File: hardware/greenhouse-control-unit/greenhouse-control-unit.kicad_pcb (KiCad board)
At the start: 4 copper layers, 150 x 90 mm, 53 parts, among them J1 Molex_KK-396_01x02, J10 Conn_ESP32_DevKitV1_Female, J11 Conn_01x05_Female, J12 Conn_01x05_Female, J13 Molex_KK-396_01x12, J14 Molex_KK-254_01x12, J2 Molex_KK-396_01x02, J3 Beep_Jumper, J4 Conn_01x01_Male, J5 Conn_01x01_Male, J6 Conn_01x01_Male, J7 Conn_01x01_Male, J8 Conn_01x09, J9 Conn_01x05_Female, Q1 BC547, Q2 BC547, Q3 BC337, Q4 BC547, Q5 2N3906, Q6 BC547, Q7 BC337, U1 PCF8574

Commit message: Add power in/out silkscreen text
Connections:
- J1 pad 1: /Batt+12V -> +12V

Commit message: Add + pin text to PCB
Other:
- board text added: "+"
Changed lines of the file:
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@@
   (gr_rect (start 104.14 104.278) (end 94.017 128.778) (layer "Dwgs.User") (width 0.15) (fill none))
   (gr_rect locked (start 72.1356 44.4645) (end 222.1356 134.4645) (layer "Edge.Cuts") (width 0.2) (fill none))
+  (gr_text "+" (at 191.7 45.538) (layer "F.SilkS")
+    (effects (font (size 1 1) (thickness 0.15)))
+  )
+  (gr_text "+" (at 142.2 45.538) (layer "F.SilkS")
+    (effects (font (size 1 1) (thickness 0.15)))
+  )
+  (gr_text "+" (at 173.95 45.538) (layer "F.SilkS")
+    (effects (font (size 1 1) (thickness 0.15)))
+  )
   (gr_text "OUT" (at 208.9284 104.1015) (layer "F.SilkS")
     (effects (font (size 1.5 1.5) (thickness 0.25)))
@@
     (effects (font (size 1.5 1.5) (thickness 0.3)) (justify left))
   )
+  (gr_text "+" (at 158.15 45.538) (layer "F.SilkS")
+    (effects (font (size 1 1) (thickness 0.15)))
+  )
+  (gr_text "+" (at 150.1 45.538) (layer "F.SilkS")
+    (effects (font (size 1 1) (thickness 0.15)))
+  )
   (gr_text "5V buck module" (at 208.806 60.706) (layer "F.SilkS")
     (effects (font (size 1.5 1.5) (thickness 0.25)))
+  )
+  (gr_text "+" (at 181.8 45.538) (layer "F.SilkS")
+    (effects (font (size 1 1) (thickness 0.15)))
   )
   (gr_text "Greenhouse Control Unit" (at 181.61 127.508) (layer "F.SilkS")
@@
     (effects (font (size 1.5 1.5) (thickness 0.25)))
   )
+  (gr_text "+" (at 201.85 45.538) (layer "F.SilkS")
+    (effects (font (size 1 1) (thickness 0.15)))
+  )
+  (gr_text "+" (at 165.85 45.538) (layer "F.SilkS")
+    (effects (font (size 1 1) (thickness 0.15)))
+  )
   (segment (start 102.616 49.53) (end 102.616 51.435) (width 0.5) (layer "F.Cu") (net 1))

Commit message: Fixed missing GND on MCU
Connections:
- J10 pad 17: unconnected-(J10-Pad17) -> GND
- J10 pad 2: unconnected-(J10-Pad2) -> GND
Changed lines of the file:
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@@
   (net 57 "Net-(J3-Pad1)")
   (net 58 "unconnected-(J3-Pad3)")
-  (net 59 "unconnected-(J10-Pad2)")
-  (net 60 "unconnected-(J10-Pad3)")
-  (net 61 "unconnected-(J10-Pad4)")
-  (net 62 "unconnected-(J10-Pad7)")
-  (net 63 "unconnected-(J10-Pad8)")
-  (net 64 "unconnected-(J10-Pad9)")
-  (net 65 "unconnected-(J10-Pad10)")
-  (net 66 "unconnected-(J10-Pad11)")
-  (net 67 "unconnected-(J10-Pad13)")
-  (net 68 "unconnected-(J10-Pad14)")
-  (net 69 "unconnected-(J10-Pad15)")
-  (net 70 "unconnected-(J10-Pad17)")
-  (net 71 "unconnected-(J10-Pad18)")
-  (net 72 "unconnected-(J10-Pad19)")
-  (net 73 "unconnected-(J10-Pad21)")
-  (net 74 "unconnected-(J10-Pad22)")
-  (net 75 "unconnected-(J10-Pad27)")
-  (net 76 "unconnected-(J10-Pad28)")
+  (net 59 "unconnected-(J10-Pad3)")
+  (net 60 "unconnected-(J10-Pad4)")
+  (net 61 "unconnected-(J10-Pad7)")
+  (net 62 "unconnected-(J10-Pad8)")
+  (net 63 "unconnected-(J10-Pad9)")
+  (net 64 "unconnected-(J10-Pad10)")
+  (net 65 "unconnected-(J10-Pad11)")
+  (net 66 "unconnected-(J10-Pad13)")
+  (net 67 "unconnected-(J10-Pad14)")
+  (net 68 "unconnected-(J10-Pad15)")
+  (net 69 "unconnected-(J10-Pad18)")
+  (net 70 "unconnected-(J10-Pad19)")
+  (net 71 "unconnected-(J10-Pad21)")
+  (net 72 "unconnected-(J10-Pad22)")
+  (net 73 "unconnected-(J10-Pad27)")
+  (net 74 "unconnected-(J10-Pad28)")
   (footprint "Connector_PinHeader_2.54mm:PinHeader_1x03_P2.54mm_Vertical" (layer "F.Cu")
     (at 91.1468 71.7296 90)
@@
       (net 3 "+5V") (pinfunction "VIN_5V") (pintype "power_in"))
     (pad "2" thru_hole oval (at -13.3 15.076 180) (size 1.7 1.7) (drill 1) (layers *.Cu *.Mask)
-      (net 59 "unconnected-(J10-Pad2)") (pinfunction "GND") (pintype "power_in+no_connect"))
+      (net 1 "GND") (pinfunction "GND") (pintype "power_in"))
     (pad "3" thru_hole oval (at -13.3 12.536 180) (size 1.7 1.7) (drill 1) (layers *.Cu *.Mask)
-      (net 60 "unconnected-(J10-Pad3)") (pinfunction "D13") (pintype "bidirectional+no_connect"))
+      (net 59 "unconnected-(J10-Pad3)") (pinfunction "D13") (pintype "bidirectional+no_connect"))
     (pad "4" thru_hole oval (at -13.3 9.996 180) (size 1.7 1.7) (drill 1) (layers *.Cu *.Mask)
-      (net 61 "unconnected-(J10-Pad4)") (pinfunction "D12") (pintype "bidirectional+no_connect"))
+      (net 60 "unconnected-(J10-Pad4)") (pinfunction "D12") (pintype "bidirectional+no_connect"))
     (pad "5" thru_hole oval (at -13.3 7.456 180) (size 1.7 1.7) (drill 1) (layers *.Cu *.Mask)
       (net 29 "/HC12_RX") (pinfunction "D14") (pintype "bidirectional"))
@@
       (net 30 "/HC12_TX") (pinfunction "D27") (pintype "bidirectional"))
     (pad "7" thru_hole oval (at -13.3 2.376 180) (size 1.7 1.7) (drill 1) (layers *.Cu *.Mask)
-      (net 62 "unconnected-(J10-Pad7)") (pinfunction "D26") (pintype "bidirectional+no_connect"))
+      (net 61 "unconnected-(J10-Pad7)") (pinfunction "D26") (pintype "bidirectional+no_connect"))
     (pad "8" thru_hole oval (at -13.3 -0.164 180) (size 1.7 1.7) (drill 1) (layers *.Cu *.Mask)
-      (net 63 "unconnected-(J10-Pad8)") (pinfunction "D25") (pintype "bidirectional+no_connect"))
+      (net 62 "unconnected-(J10-Pad8)") (pinfunction "D25") (pintype "bidirectional+no_connect"))
     (pad "9" thru_hole oval (at -13.3 -2.704 180) (size 1.7 1.7) (drill 1) (layers *.Cu *.Mask)
-      (net 64 "unconnected-(J10-Pad9)") (pinfunction "D33") (pintype "bidirectional+no_connect"))
+      (net 63 "unconnected-(J10-Pad9)") (pinfunction "D33") (pintype "bidirectional+no_connect"))
     (pad "10" thru_hole oval (at -13.3 -5.244 180) (size 1.7 1.7) (drill 1) (layers *.Cu *.Mask)
-      (net 65 "unconnected-(J10-Pad10)") (pinfunction "D32") (pintype "bidirectional+no_connect"))
+      (net 64 "unconnected-(J10-Pad10)") (pinfunction "D32") (pintype "bidirectional+no_connect"))
     (pad "11" thru_hole oval (at -13.3 -7.784 180) (size 1.7 1.7) (drill 1) (layers *.Cu *.Mask)
-      (net 66 "unconnected-(J10-Pad11)") (pinfunction "D35") (pintype "bidirectional+no_connect"))
+      (net 65 "unconnected-(J10-Pad11)") (pinfunction "D35") (pintype "bidirectional+no_connect"))
     (pad "12" thru_hole oval (at -13.3 -10.324 180) (size 1.7 1.7) (drill 1) (layers *.Cu *.Mask)
       (net 31 "/VSense") (pinfunction "D34") (pintype "bidirectional"))
     (pad "13" thru_hole oval (at -13.3 -12.864 180) (size 1.7 1.7) (drill 1) (layers *.Cu *.Mask)
-      (net 67 "unconnected-(J10-Pad13)") (pinfunction "VN") (pintype "bidirectional+no_connect"))
+      (net 66 "unconnected-(J10-Pad13)") (pinfunction "VN") (pintype "bidirectional+no_connect"))
     (pad "14" thru_hole oval (at -13.3 -15.404 180) (size 1.7 1.7) (drill 1) (layers *.Cu *.Mask)
-      (net 68 "unconnected-(J10-Pad14)") (pinfunction "VP") (pintype "bidirectional+no_connect"))
+      (net 67 "unconnected-(J10-Pad14)") (pinfunction "VP") (pintype "bidirectional+no_connect"))
     (pad "15" thru_hole oval (at -13.3 -17.944 180) (size 1.7 1.7) (drill 1) (layers *.Cu *.Mask)
-      (net 69 "unconnected-(J10-Pad15)") (pinfunction "EN") (pintype "bidirectional+no_connect"))
+      (net 68 "unconnected-(J10-Pad15)") (pinfunction "EN") (pintype "bidirectional+no_connect"))
     (pad "16" thru_hole rect (at 12.4 17.616 180) (size 1.7 1.7) (drill 1) (layers *.Cu *.Mask)
       (net 4 "+3V3") (pinfunction "3V3") (pintype "power_out"))
     (pad "17" thru_hole oval (at 12.4 15.086) (size 1.7 1.7) (drill 1) (layers *.Cu *.Mask)
-      (net 70 "unconnected-(J10-Pad17)") (pinfunction "GND") (pintype "power_in+no_connect"))
+      (net 1 "GND") (pinfunction "GND") (pintype "power_in"))
     (pad "18" thru_hole oval (at 12.4 12.546) (size 1.7 1.7) (drill 1) (layers *.Cu *.Mask)
-      (net 71 "unconnected-(J10-Pad18)") (pinfunction "D15") (pintype "bidirectional+no_connect"))
+      (net 69 "unconnected-(J10-Pad18)") (pinfunction "D15") (pintype "bidirectional+no_connect"))
     (pad "19" thru_hole oval (at 12.4 10.006) (size 1.7 1.7) (drill 1) (layers *.Cu *.Mask)
-      (net 72 "unconnected-(J10-Pad19)") (pinfunction "D2") (pintype "bidirectional+no_connect"))
+      (net 70 "unconnected-(J10-Pad19)") (pinfunction "D2") (pintype "bidirectional+no_connect"))
     (pad "20" thru_hole oval (at 12.4 7.466) (size 1.7 1.7) (drill 1) (layers *.Cu *.Mask)
       (net 24 "/RFM95_IRQ") (pinfunction "D4") (pintype "bidirectional"))
     (pad "21" thru_hole oval (at 12.4 4.926) (size 1.7 1.7) (drill 1) (layers *.Cu *.Mask)
-      (net 73 "unconnected-(J10-Pad21)") (pinfunction "RX2") (pintype "bidirectional+no_connect"))
+      (net 71 "unconnected-(J10-Pad21)") (pinfunction "RX2") (pintype "bidirectional+no_connect"))
     (pad "22" thru_hole oval (at 12.4 2.386) (size 1.7 1.7) (drill 1) (layers *.Cu *.Mask)
-      (net 74 "unconnected-(J10-Pad22)") (pinfunction "TX2") (pintype "bidirectional+no_connect"))
+      (net 72 "unconnected-(J10-Pad22)") (pinfunction "TX2") (pintype "bidirectional+no_connect"))
     (pad "23" thru_hole oval (at 12.4 -0.154) (size 1.7 1.7) (drill 1) (layers *.Cu *.Mask)
       (net 28 "/RFM95_CS") (pinfunction "D5") (pintype "bidirectional"))
@@
       (net 22 "/I2C_SDA") (pinfunction "D21") (pintype "bidirectional"))
     (pad "27" thru_hole oval (at 12.4 -10.314) (size 1.7 1.7) (drill 1) (layers *.Cu *.Mask)
-      (net 75 "unconnected-(J10-Pad27)") (pinfunction "RXD") (pintype "bidirectional+no_connect"))
+      (net 73 "unconnected-(J10-Pad27)") (pinfunction "RXD") (pintype "bidirectional+no_connect"))
     (pad "28" thru_hole oval (at 12.4 -12.854) (size 1.7 1.7) (drill 1) (layers *.Cu *.Mask)
-      (net 76 "unconnected-(J10-Pad28)") (pinfunction "TXD") (pintype "bidirectional+no_connect"))
+      (net 74 "unconnected-(J10-Pad28)") (pinfunction "TXD") (pintype "bidirectional+no_connect"))
     (pad "29" thru_hole oval (at 12.4 -15.394) (size 1.7 1.7) (drill 1) (layers *.Cu *.Mask)
       (net 23 "/I2C_SCL") (pinfunction "D22") (pintype "bidirectional"))

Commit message: First pass at R4
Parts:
- removed C1: 220uF, Capacitor_THT:CP_Radial_D6.3mm_P2.50mm
- removed J13: Molex_KK-396_01x12, Connector_Molex:Molex_KK-396_A-41791-0012_1x12_P3.96mm_Vertical
- removed J7: Conn_01x01_Male, Connector_Pin:Pin_D1.0mm_L10.0mm
- added C3: 10nF, Capacitor_THT:C_Disc_D4.7mm_W2.5mm_P5.00mm, F.Cu at (137.7, 83.1)
- added F1: Fuse, Fuse:Fuse_Blade_Mini_directSolder, F.Cu at (170.6, 39.1)
- added J15: Molex_KK-396_01x02, Connector_Molex:Molex_KK-396_A-41791-0002_1x02_P3.96mm_Vertical, F.Cu at (199.4, 42.2)
- added Q10: 2N7000, Package_TO_SOT_THT:TO-92_Inline, F.Cu at (110.0, 88.5)
- added Q11: FDP7030BL, Package_TO_SOT_THT:TO-220-3_Horizontal_TabDown, F.Cu at (212.6, 54.3)
- added Q12: FDP7030BL, Package_TO_SOT_THT:TO-220-3_Horizontal_TabDown, F.Cu at (167.9, 54.3)
- added Q13: 2N7002, Package_TO_SOT_SMD:SOT-23, F.Cu at (128.0, 64.4)
- added Q14: STD30NF06LT4, Package_TO_SOT_SMD:TO-252-2, F.Cu at (128.0, 56.1)
- added Q15: 2N7002, Package_TO_SOT_SMD:SOT-23, F.Cu at (143.3, 64.4)
- added Q16: STD30NF06LT4, Package_TO_SOT_SMD:TO-252-2, F.Cu at (143.3, 56.1)
- added Q17: 2N7002, Package_TO_SOT_SMD:SOT-23, F.Cu at (135.6, 64.4)
- added Q18: 2N7002, Package_TO_SOT_SMD:SOT-23, F.Cu at (150.9, 64.4)
- added Q19: STD30NF06LT4, Package_TO_SOT_SMD:TO-252-2, F.Cu at (135.6, 56.1)
- added Q20: STD30NF06LT4, Package_TO_SOT_SMD:TO-252-2, F.Cu at (150.9, 56.1)
- added Q8: FDP7030BL, Package_TO_SOT_THT:TO-220-3_Horizontal_TabDown, F.Cu at (201.4, 54.3)
- added Q9: FDP7030BL, Package_TO_SOT_THT:TO-220-3_Horizontal_TabDown, F.Cu at (179.1, 54.3)
- added R18: 0R1, Resistor_SMD:R_2512_6332Metric_Pad1.40x3.35mm_HandSolder, F.Cu at (159.8, 46.0)
- added R19: 10k, Resistor_THT:R_Axial_DIN0207_L6.3mm_D2.5mm_P7.62mm_Horizontal, F.Cu at (111.5, 58.2)
- added R20: 10k, Resistor_THT:R_Axial_DIN0207_L6.3mm_D2.5mm_P7.62mm_Horizontal, F.Cu at (99.3, 50.5)
- added R21: 10k, Resistor_THT:R_Axial_DIN0207_L6.3mm_D2.5mm_P7.62mm_Horizontal, F.Cu at (125.5, 83.1)
- added R22: 100k, Resistor_THT:R_Axial_DIN0207_L6.3mm_D2.5mm_P7.62mm_Horizontal, F.Cu at (129.7, 75.8)
- added R23: 10k, Resistor_THT:R_Axial_DIN0207_L6.3mm_D2.5mm_P7.62mm_Horizontal, F.Cu at (108.5, 58.2)
- added R24: 1M, Resistor_THT:R_Axial_DIN0207_L6.3mm_D2.5mm_P7.62mm_Horizontal, F.Cu at (105.4, 50.5)
- added R25: 100k, Resistor_THT:R_Axial_DIN0207_L6.3mm_D2.5mm_P7.62mm_Horizontal, F.Cu at (102.4, 58.2)
- added R26: 10k, Resistor_THT:R_Axial_DIN0207_L6.3mm_D2.5mm_P7.62mm_Horizontal, F.Cu at (96.3, 50.5)
- added R27: 10k, Resistor_THT:R_Axial_DIN0207_L6.3mm_D2.5mm_P7.62mm_Horizontal, F.Cu at (126.4, 68.2)
- added R28: 100k, Resistor_THT:R_Axial_DIN0207_L6.3mm_D2.5mm_P7.62mm_Horizontal, F.Cu at (144.9, 75.9)
- added R29: 10k, Resistor_THT:R_Axial_DIN0207_L6.3mm_D2.5mm_P7.62mm_Horizontal, F.Cu at (141.6, 68.2)
- added R30: 100k, Resistor_THT:R_Axial_DIN0207_L6.3mm_D2.5mm_P7.62mm_Horizontal, F.Cu at (137.3, 75.8)
- added R31: 100k, Resistor_THT:R_Axial_DIN0207_L6.3mm_D2.5mm_P7.62mm_Horizontal, F.Cu at (152.5, 75.8)
- added R32: 10k, Resistor_THT:R_Axial_DIN0207_L6.3mm_D2.5mm_P7.62mm_Horizontal, F.Cu at (134.0, 68.2)
- added R33: 10k, Resistor_THT:R_Axial_DIN0207_L6.3mm_D2.5mm_P7.62mm_Horizontal, F.Cu at (149.2, 68.2)
- added U2: PCF8574, Package_SO:SOIC-16W_7.5x10.3mm_P1.27mm, F.Cu at (135.2, 90.2)
- added U3: ZXCT1107, Package_TO_SOT_SMD:SOT-23, F.Cu at (213.9, 49.5)
- added U4: ZXCT1107, Package_TO_SOT_SMD:SOT-23, F.Cu at (159.8, 50.0)
- D4: value LED -> D; footprint LED_THT:LED_D5.0mm -> Diode_THT:D_DO-41_SOD81_P7.62mm_Horizontal
- D5: value FR107 -> LED; footprint Diode_THT:D_DO-41_SOD81_P7.62mm_Horizontal -> LED_THT:LED_D5.0mm
- J4: value Conn_01x01_Male -> PV Buck; footprint Connector_Pin:Pin_D1.0mm_L10.0mm -> Nick:Buck_Module
- J5: value Conn_01x01_Male -> Conn_01x08_Male; footprint Connector_Pin:Pin_D1.0mm_L10.0mm -> Connector_Molex:Molex_KK-396_A-41791-0008_1x08_P3.96mm_Vertical
- J6: value Conn_01x01_Male -> 5V Buck; footprint Connector_Pin:Pin_D1.0mm_L10.0mm -> Nick:Buck_Module
- Q1, Q4: value BC547 -> 2N7000
- Q3: value BC337 -> TN0702
- Q5: value 2N3906 -> FDP7030BL; footprint Package_TO_SOT_THT:TO-92_Inline -> Package_TO_SOT_THT:TO-220-3_Horizontal_TabDown
- R1: value 33k -> 100k
- R10: value 220k -> 100k
- R12: value 10k -> 0R1; footprint Resistor_THT:R_Axial_DIN0207_L6.3mm_D2.5mm_P7.62mm_Horizontal -> Resistor_SMD:R_2512_6332Metric_Pad1.40x3.35mm_HandSolder
- R3, R8: value 1k -> 10k
- U1: footprint Package_DIP:DIP-16_W7.62mm_Socket -> Package_SO:SOIC-16W_7.5x10.3mm_P1.27mm
- moved D4 139.8 mm to (216.7, 78.2), turned to 180 degrees
- moved J5 94.5 mm to (125.2, 42.4), turned to 0 degrees
- moved R12 86.9 mm to (217.9, 49.5)
- moved Q5 86.9 mm to (190.2, 54.3), turned to 180 degrees
- moved D6 26.9 mm to (193.5, 78.2), turned to 180 degrees
- moved U1 25.4 mm to (135.2, 104.4)
- moved D5 25.0 mm to (77.6, 67.6), turned to -90 degrees
- moved C2 19.9 mm to (137.7, 97.3), turned to 180 degrees
- moved R9 19.7 mm to (114.6, 50.5)
- moved R10 19.5 mm to (117.7, 58.2)
- moved R3 18.9 mm to (117.9, 95.2), turned to 0 degrees
- moved Q4 17.6 mm to (103.6, 88.5)
- moved R16 16.3 mm to (117.9, 98.3)
- moved R5 16.3 mm to (125.5, 92.2)
- moved J1 15.3 mm to (189.5, 42.3)
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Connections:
- net /VSense renamed /Common_VS
- D4 pad 1: GND -> Net-(D4-Pad1)
- D4 pad 2: Net-(D4-Pad2) -> /PV_Vcc
- D5 pad 1: /BattRelayNC_A -> GND
- D5 pad 2: GND -> Net-(D5-Pad2)
- D6 pad 1: /Buck+12V -> Net-(D6-Pad1)
- J1 pad 1: +12V -> /Batt+12V
- J1 pad 2: GND -> /Batt_GND
- J10 pad 10: unconnected-(J10-Pad10) -> /PV_PWM
- J10 pad 11: unconnected-(J10-Pad11) -> /PV_VS
- J10 pad 8: unconnected-(J10-Pad8) -> /PV_IS
- J10 pad 9: unconnected-(J10-Pad9) -> /Common_IS
- J14 pad 6: /BattRelayNC_A -> unconnected-(J14-Pad6)
- J14 pad 7: GND -> unconnected-(J14-Pad7)
- J2 pad 1: +12V -> /Common+12V
- J2 pad 2: GND -> /PSU_GND
- J4 pad 1: +5V -> Net-(D4-Pad1)
- J5 pad 1: /Buck+12V -> +12V
- J6 pad 1: GND -> Net-(D6-Pad1)
- J8 pad 3: /RFM95_EN -> unconnected-(J8-Pad3)
- Q1 pad 1: Net-(C1-Pad1) -> GND
- Q1 pad 2: Net-(Q1-Pad2) -> /IO_Beep
- Q1 pad 3: GND -> Net-(Q1-Pad3)
- Q3 pad 1: Net-(BZ1-Pad2) -> GND
- Q3 pad 2: Net-(C1-Pad1) -> Net-(Q1-Pad3)
- Q3 pad 3: GND -> Net-(BZ1-Pad2)
- Q4 pad 1: Net-(Q4-Pad1) -> /IO_PSU_EN
- Q4 pad 2: +3V3 -> Net-(Q4-Pad2)
- Q5 pad 1: +12V -> Net-(Q4-Pad3)
- Q5 pad 2: Net-(Q4-Pad1) -> Net-(Q5-Pad2)
- Q5 pad 3: /BattRelayNC_A -> /PSU_GND
- R1 pad 2: Net-(Q1-Pad2) -> +3V3
- R12 pad 1: +12V -> /Batt+12V
- R12 pad 2: Net-(D4-Pad2) -> /PV_Buck_Vcc
- R2 pad 1: /IO_PsuRelay_EN -> /IO_AC_EN
- R3 pad 1: +5V -> Net-(Q1-Pad3)
- R3 pad 2: Net-(C1-Pad1) -> +5V
- R8 pad 1: /IO_Batt_EN -> +3V3
- R8 pad 2: Net-(Q4-Pad3) -> Net-(Q4-Pad2)
- U1 pad 10: /IO_PsuLed -> /IO_PSU_EN
- U1 pad 11: unconnected-(U1-Pad11) -> /IO_AC_EN
- U1 pad 4: /IO_Batt_EN -> /IO_CaseFan_EN
- U1 pad 5: /IO_PsuRelay_EN -> /IO_Beep
- U1 pad 6: /IO_Beep -> /IO_PsuLed
- U1 pad 7: /IO_CaseFan_EN -> /IO_BatteryLed
- U1 pad 9: /IO_BatteryLed -> /IO_Batt_EN
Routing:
- net /PV_GND: track 0.00 -> 171.1 mm, vias 0 -> 1
- net /PV_PWM: track 0.00 -> 168.3 mm, vias 0 -> 1
- net /PV_Vcc: track 0.00 -> 165.9 mm, vias 0 -> 1
- net Net-(Q4-Pad3): track 14.6 -> 136.4 mm, vias 0 -> 1
- net /PV_IS: track 0.00 -> 114.6 mm, vias 0 -> 1
- net Net-(Q10-Pad3): track 0.00 -> 105.9 mm, vias 0 -> 1
- net /PV_Buck_Vcc: track 0.00 -> 76.7 mm
- net +3V3: track 3.81 -> 75.4 mm
- net /Common_IS: track 0.00 -> 65.6 mm, vias 0 -> 1
- net /IO_Batt_EN: track 7.11 -> 70.2 mm, vias 0 -> 1
- net /Batt_GND: track 0.00 -> 61.9 mm
- net /PV_VS: track 0.00 -> 59.4 mm
- net /IO_PSU_EN: track 0.00 -> 59.4 mm, vias 0 -> 1
- net Net-(D4-Pad2): track 54.3 -> 0.00 mm
- net /IO_OUT_4: track 0.00 -> 50.0 mm
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- added copper zone on F.Cu, net +12V
- added copper zone on F.Cu, net /Batt+12V
- added copper zone on F.Cu, net /Common+12V
- added copper zone on F.Cu, net GND
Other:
- board size 150 x 90 mm -> 150 x 99.9 mm
- board text added: "Greenhouse Control Unit R4 Nick Bolton"
- board text removed: "5V buck module"
- board text removed: "Greenhouse Control Unit"
- board text removed: "IN"
- board text removed: "Nick Bolton"
- board text removed: "OUT"

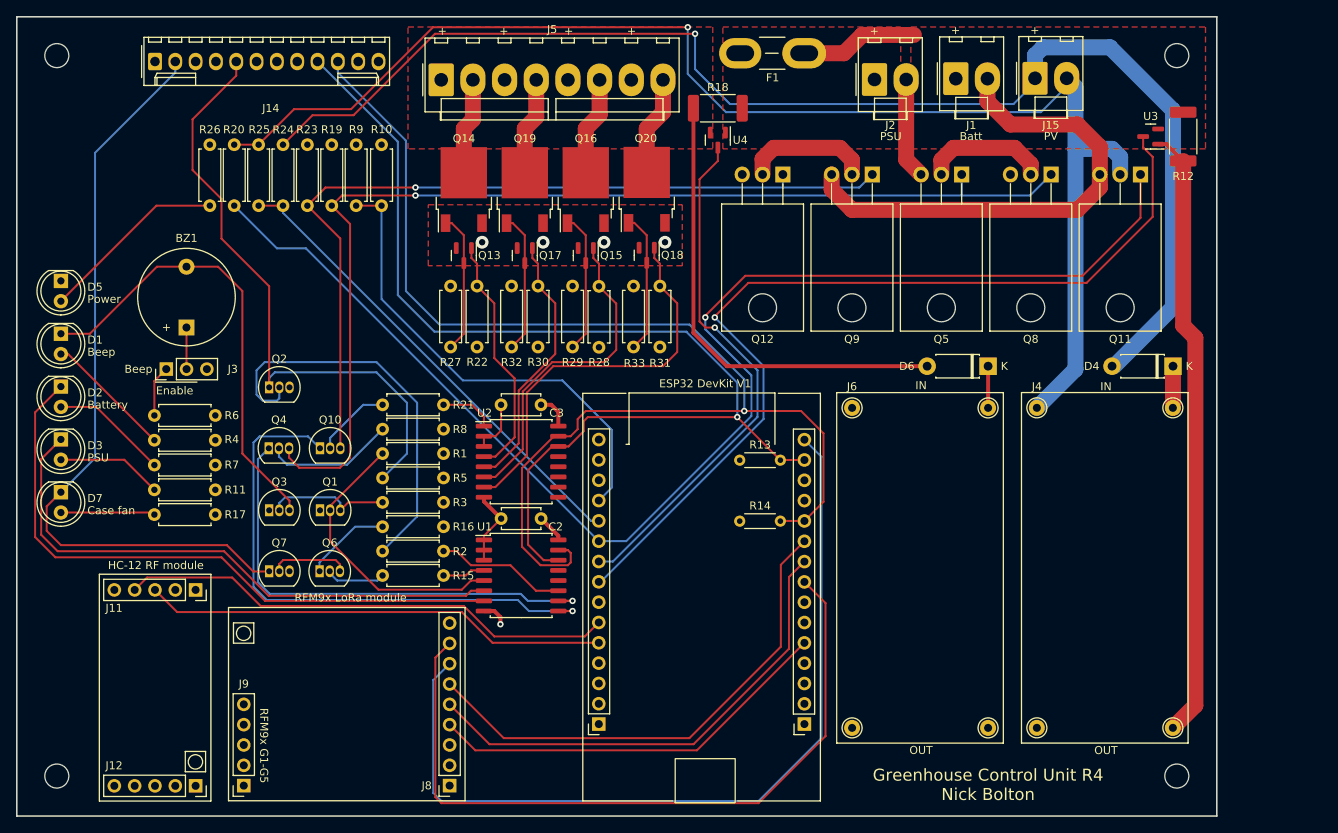
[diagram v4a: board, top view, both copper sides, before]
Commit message: Optimized power use and moved beeper
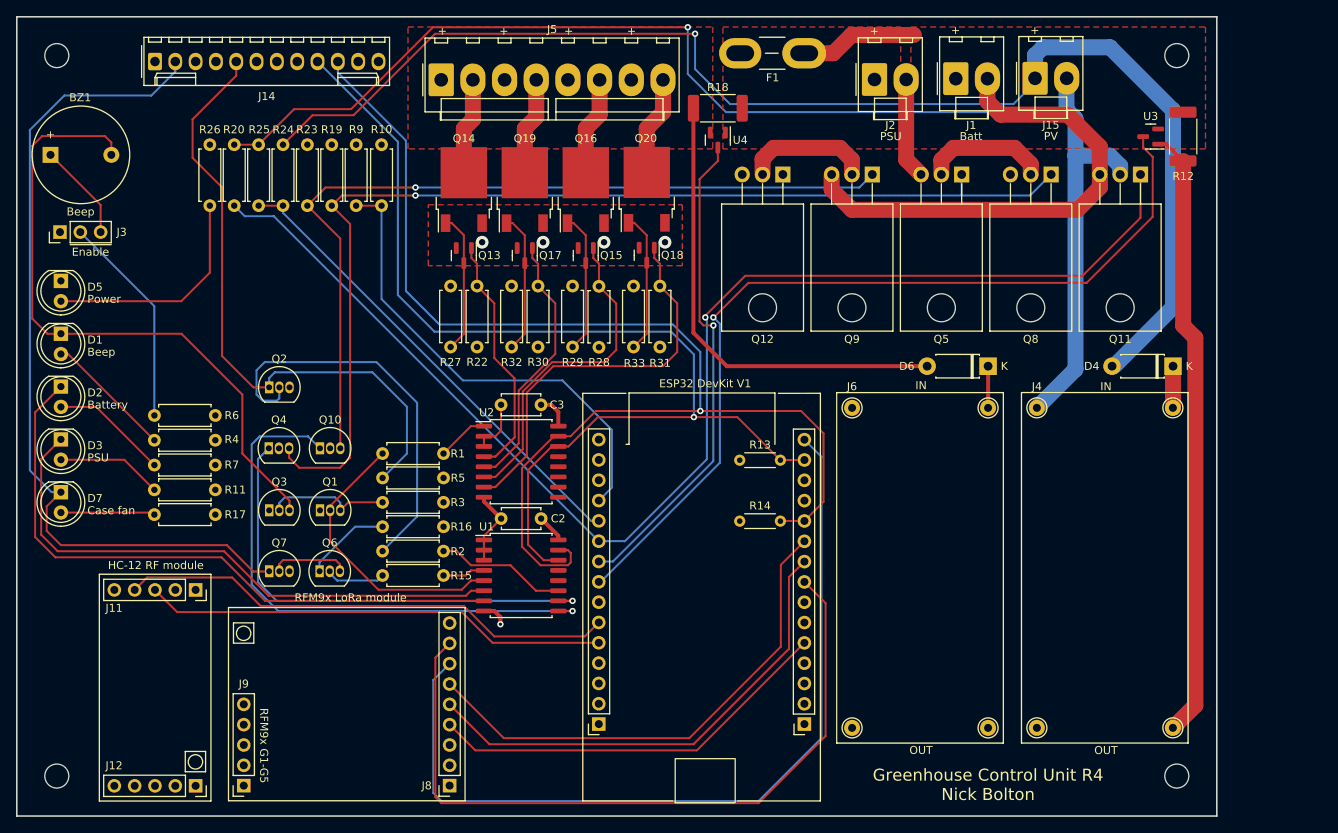
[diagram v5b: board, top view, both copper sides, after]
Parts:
- removed R21, R8: 10k, Resistor_THT:R_Axial_DIN0207_L6.3mm_D2.5mm_P7.62mm_Horizontal
- R27, R29, R32, R33: value 10k -> 100k
- moved BZ1 27.5 mm to (76.4, 51.8), turned to 0 degrees
- moved J3 21.7 mm to (77.5, 61.5)
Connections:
- J3 pad 1: Net-(J3-Pad1) -> unconnected-(J3-Pad1)
- J3 pad 2: Net-(BZ1-Pad1) -> Net-(R6-Pad2)
- J3 pad 3: unconnected-(J3-Pad3) -> Net-(BZ1-Pad1)
- Q10 pad 2: Net-(Q10-Pad2) -> +3V3
- Q4 pad 2: Net-(Q4-Pad2) -> +3V3
- R6 pad 2: Net-(J3-Pad1) -> Net-(R6-Pad2)
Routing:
- net Net-(R6-Pad2): track 0.00 -> 26.8 mm
- net Net-(BZ1-Pad2): track 57.3 -> 80.9 mm
- net Net-(Q4-Pad2): track 16.3 -> 0.00 mm
- net /CaseFan_Sink: track 95.4 -> 105.6 mm
- net Net-(Q10-Pad2): track 9.57 -> 0.00 mm
- net +3V3: track 75.4 -> 67.9 mm
- net Net-(BZ1-Pad1): track 5.19 -> 12.2 mm
- net Net-(J3-Pad1): track 6.41 -> 0.00 mm
- net Net-(D5-Pad2): track 23.6 -> 28.5 mm
- net /PV_PWM: track 168.3 -> 163.6 mm
- net /Common_IS: track 65.6 -> 61.1 mm
- net /PV_IS: track 114.6 -> 110.2 mm
- net /I2C_SDA: track 159.8 -> 155.6 mm
- net /I2C_SCL: track 137.9 -> 133.8 mm
- net /PsuRelayNC_IN: track 77.9 -> 78.7 mm
